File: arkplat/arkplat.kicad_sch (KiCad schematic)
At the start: 1 part, among them U1 portenta

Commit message: wip on poe
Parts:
- removed U1: portenta, custom_footprints:portenta, symbol cusom_symbols:portenta
- added BT1: Battery_Cell, Battery:BatteryHolder_Keystone_3034_1x20mm, symbol Device:Battery_Cell
- added C1, C2, C3, C4: 100nF, Capacitor_SMD:C_0603_1608Metric, symbol Device:C_Small
- added C5, C6, C7, C8: 0.039uF, Capacitor_SMD:C_0603_1608Metric, symbol Device:C_Small
- added C9: 1000pF, Capacitor_SMD:C_1206_3216Metric, symbol Device:C_Small
- added D1, D2, D3, D4, D5, D6, D7, D8: D_Schottky, Diode_SMD:D_SMC, symbol Device:D_Schottky
- added J1: portenta_HD_J1, custom_footprints:DF40HC(3.5)-80DS-0.4V(51), symbol cusom_symbols:portenta_HD_J1
- added J2: portenta_HD_J2, custom_footprints:DF40HC(3.5)-80DS-0.4V(51), symbol cusom_symbols:portenta_HD_J2
- added J3: Conn_02x05_Odd_Even, Connector_PinHeader_1.27mm:PinHeader_2x05_P1.27mm_Vertical_SMD, symbol Connector_Generic:Conn_02x05_Odd_Even
- added J4: Conn_01x04, Connector_PinHeader_2.54mm:PinHeader_1x04_P2.54mm_Vertical, symbol Connector_Generic:Conn_01x04
- added J5: RJ45_LED_Shielded, Connector_RJ:RJ45_Amphenol_RJHSE538X, symbol Connector:RJ45_LED_Shielded
- added LOGO1, LOGO2: Logo_Open_Hardware_Small, custom_footprints:logo, symbol Graphic:Logo_Open_Hardware_Small
- added R1, R2: 470, Resistor_SMD:R_0603_1608Metric, symbol Device:R_Small_US
- added R3, R4, R5, R6: 75, Resistor_SMD:R_0603_1608Metric, symbol Device:R_Small_US
- added SW1: SW_DIP_x02, Button_Switch_SMD:SW_DIP_SPSTx02_Slide_Omron_A6H-2101_W6.15mm_P1.27mm, symbol Switch:SW_DIP_x02
- added SW2: SW_Push, Button_Switch_SMD:SW_SPST_PTS645, symbol Switch:SW_Push
- added SYM1: SYM_Flash_Small, custom_footprints:portenta, symbol Graphic:SYM_Flash_Small
- added TR1: TG111-MSC13LF, Transformer_SMD:Transformer_Ethernet_HALO_TG111-MSC13, symbol Transformer:TG111-MSC13LF
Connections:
- new net: C6.1, R5.2
- new net: J1.49 (CAN1_TX), J4.2 (Pin_2)
- new net: J1.51 (CAN1_RX), J4.3 (Pin_3)
- new net: C7.1, R6.2
- new net: C9.2, R3.1, R4.1, R5.1, R6.1
- new net: J5.7, TR1.11 (TD4+)
- new net: J5.8, TR1.12 (TD4-)
- new net: J5.1, TR1.2 (TD1+)
- new net: J5.2, TR1.3 (TD1-)
- new net: J5.3, TR1.5 (TD2+)
- new net: J5.6, TR1.6 (TD2-)
- new net: J5.4, TR1.8 (TD3+)
- new net: J5.5, TR1.9 (TD3-)
- new net: J5.10, R1.2
- new net: J5.11, R2.2
- new net: BT1.1 (+), J2.7 (COINCELL)
- new net: C8.1, R3.2
- new net: J2.1 (FORCE_BOOTLOADER), SW1.1
- new net: J2.3 (BOOT_SOURCE), SW1.2
- new net: J2.5 (POWER_ON_REQ), SW2.1
- new net: J1.73 (RESET), J3.10 (Pin_10)
- new net: J1.75 (SWDIO), J3.2 (Pin_2)
- new net: J1.77 (SWCK), J3.4 (Pin_4)
- new net: J1.79 (SWO), J3.6 (Pin_6)
- new net: C5.1, R4.2
- new net +3V3: C1.2, C2.2, C3.2, C4.2, J2.23 (VCC/+3V3), J2.34 (VCC), J2.43 (VCC/+3V3), J2.69 (VCC/+3V3), J3.1 (Pin_1), R1.1, SW1.3, SW1.4, TR1.15 (MCT4), TR1.18 (MCT3), TR1.21 (MCT2), TR1.24 (MTC1)
- new net +5V: J1.21 (VIN), J1.32 (VIN), J1.41 (VIN), J1.48 (VIN), J4.1 (Pin_1)
- new net ETH_L1: J1.17 (ETH_L1), J5.9
- new net ETH_L2: J1.19 (ETH_L2), J5.12
- new net Earth: C9.1, J5.SH
- new net GND: BT1.2 (-), C1.1, C2.1, C3.1, C4.1, J1.22 (GND), J1.31 (GND), J1.42 (GND), J1.47 (GND), J1.54 (GND), J2.24 (GND), J2.33 (GND), J2.44 (GND), J2.57 (GND), J2.70 (GND), J3.3 (Pin_3), J3.5 (Pin_5), J3.9 (Pin_9), J4.4 (Pin_4), R2.1, SW2.2
- new net PAIR1+: J1.9 (RSVD), TR1.16 (MTX3-)
- new net PAIR1-: J1.11 (RSVD), TR1.17 (MTX3+)
- new net PAIR2+: J1.1 (ETH_A+), TR1.23 (MTX1+)
- new net PAIR2-: J1.3 (ETH_A-), TR1.22 (MTX1-)
- new net PAIR3+: J1.5 (ETH_B+), TR1.20 (MTX2+)
- new net PAIR3-: J1.7 (ETH_B-), TR1.19 (MTX2-)
- new net PAIR4+: J1.13 (RSVD), TR1.14 (MX4+)
- new net PAIR4-: J1.15 (RSVD), TR1.13 (MX4-)
- new net POE+: D2.1 (K), D4.1 (K), D6.1 (K), D8.1 (K)
- new net POE-: D1.2 (A), D3.2 (A), D5.2 (A), D7.2 (A)
- new net POE_V1+: C8.2, D1.1 (K), D2.2 (A), TR1.1 (TCT1)
- new net POE_V1-: C7.2, D3.1 (K), D4.2 (A), TR1.4 (TCT2)
- new net POE_V2+: C6.2, D5.1 (K), D6.2 (A), TR1.7 (TCT3)
- new net POE_V2-: C5.2, D7.1 (K), D8.2 (A), TR1.10 (TCT4)
- no-connect marks 0 -> 2
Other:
- company: (none) -> grey@christoforo.net
- title: (none) -> Kra Platform

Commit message: wip on arkplat
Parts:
- added FL? (x2): Choke_Schaffner_RN102-1-02-3M0, Inductor_THT:Choke_Schaffner_RN102-04-14.0x14.0mm, symbol Filter:Choke_Schaffner_RN102-1-02-3M0
- added TR2: 30F-51NL, Transformer_SMD:Transformer_Ethernet_YDS_30F-51NL_SO-24_7.1x15.1mm, symbol Transformer:30F-51NL
- added U? (x4): WE-TVS-82400102, Package_TO_SOT_SMD:SOT-23-6, symbol Power_Protection:WE-TVS-82400102
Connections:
- net +3V3: now also U?.5, U?.5, U?.5, U?.5; no longer TR1.15 (MCT4), TR1.18 (MCT3), TR1.21 (MCT2), TR1.24 (MTC1)
- net GND: now also U?.2, U?.2, U?.2, U?.2
- net PAIR1+: now also U?.4; no longer TR1.16 (MTX3-)
- net PAIR1-: now also U?.6; no longer TR1.17 (MTX3+)
- net PAIR2+: now also U?.6; no longer TR1.23 (MTX1+)
- net PAIR2-: now also U?.4; no longer TR1.22 (MTX1-)
- net PAIR3+: now also U?.4; no longer TR1.20 (MTX2+)
- net PAIR3-: now also U?.6; no longer TR1.19 (MTX2-)
- net PAIR4+: now also U?.6; no longer TR1.14 (MX4+)
- net PAIR4-: now also U?.4; no longer TR1.13 (MX4-)
- net POE_V1+: now also FL?.4, TR2.10 (CT); no longer D1.1 (K), D2.2 (A), TR1.1 (TCT1)
- net POE_V1-: now also FL?.2, TR2.7 (CT); no longer D3.1 (K), D4.2 (A), TR1.4 (TCT2)
- net POE_V2+: now also FL?.4, TR2.4 (CT); no longer D5.1 (K), D6.2 (A), TR1.7 (TCT3)
- net POE_V2-: now also FL?.2, TR2.1 (CT); no longer D7.1 (K), D8.2 (A), TR1.10 (TCT4)
- net at TR1.11 (TD4+): no longer J5.7
- net at TR1.12 (TD4-): no longer J5.8
- net at TR1.2 (TD1+): no longer J5.1
- net at TR1.3 (TD1-): no longer J5.2
- net at TR1.5 (TD2+): no longer J5.3
- net at TR1.6 (TD2-): no longer J5.6
- net at TR1.8 (TD3+): no longer J5.4
- net at TR1.9 (TD3-): no longer J5.5
- new net: D1.1 (K), D2.2 (A), FL?.3
- new net: J5.1, TR2.12 (TD4-)
- new net: J5.2, TR2.11 (TD4+)
- new net: J5.3, TR2.9 (TD3-)
- new net: J5.4, TR2.6 (TD2-)
- new net: J5.5, TR2.5 (TD2+)
- new net: J5.6, TR2.8 (TD3+)
- new net: J5.7, TR2.3 (TD1-)
- new net: J5.8, TR2.2 (TD1+)
- new net: D3.1 (K), D4.2 (A), FL?.1
- new net: D5.1 (K), D6.2 (A), FL?.3
- new net: D7.1 (K), D8.2 (A), FL?.1
- no-connect marks 2 -> 10
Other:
- moved on the sheet: TR1

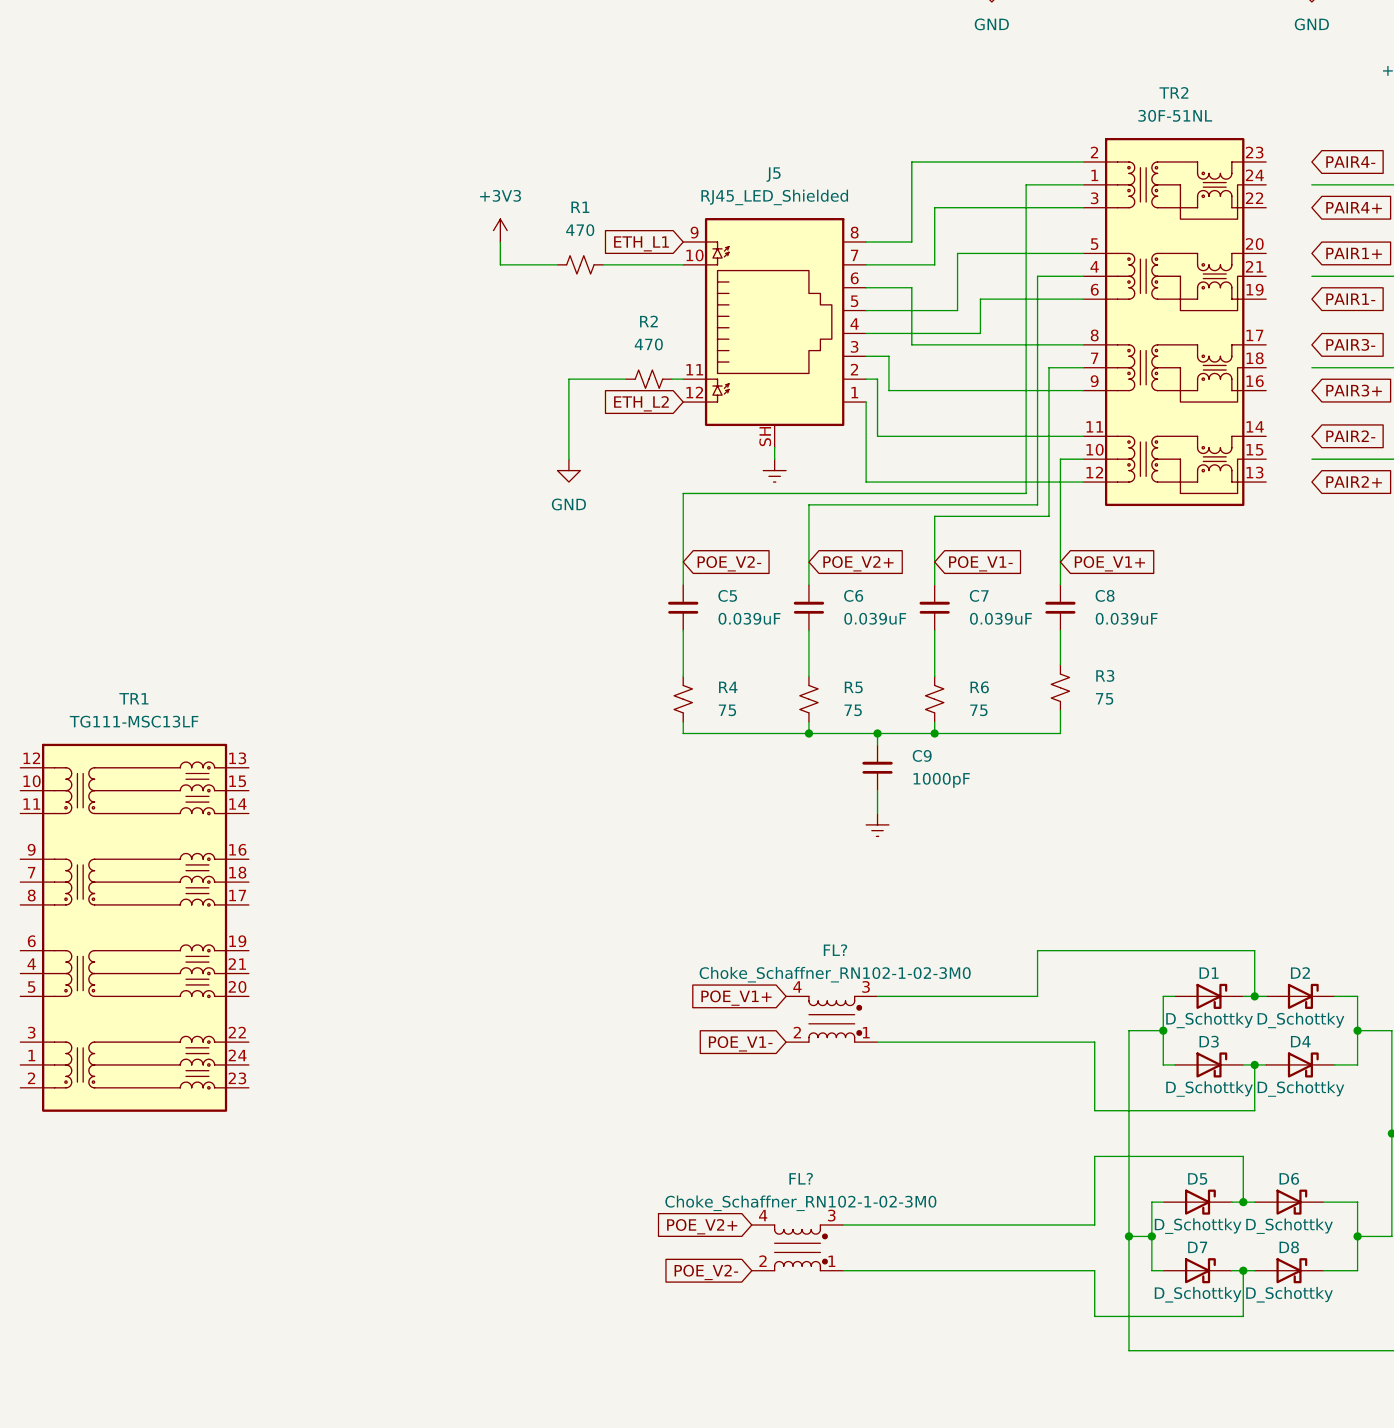
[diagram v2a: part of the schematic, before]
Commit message: rev up fourch lights, add distroboard
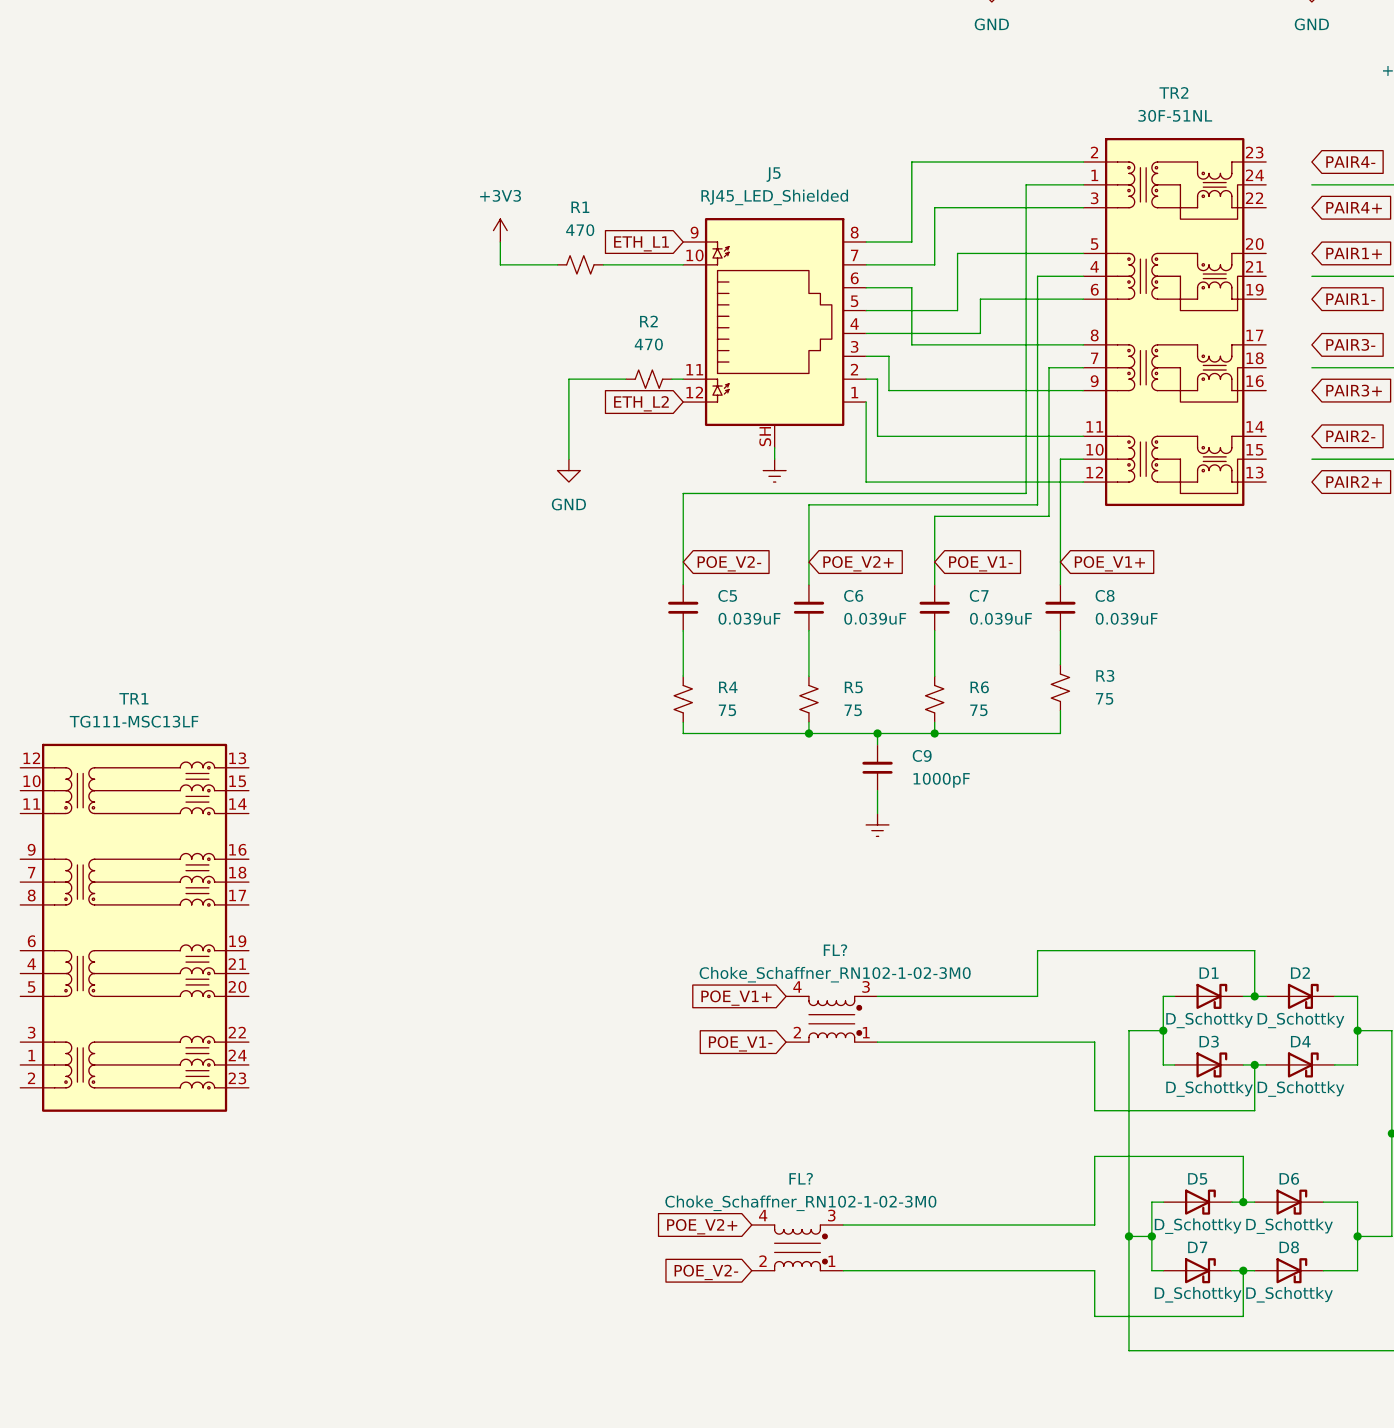
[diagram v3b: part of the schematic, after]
